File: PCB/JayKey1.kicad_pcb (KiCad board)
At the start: 2 copper layers, 419.1 x 99.4 mm, 204 parts, among them J1 USB_C_Receptacle, K0,0 KEYSW, K0,1 KEYSW, K0,10 KEYSW, K0,11 KEYSW, K0,12 KEYSW, K0,13 KEYSW, K0,14 KEYSW, K0,15 KEYSW, K0,16 KEYSW, K0,17 KEYSW, K0,18 KEYSW, K0,19 KEYSW, K0,2 KEYSW, K0,20 KEYSW, K0,3 KEYSW, K0,4 KEYSW, K0,5 KEYSW, K0,6 KEYSW, K0,7 KEYSW, K0,8 KEYSW, K0,9 KEYSW, K1,0 KEYSW, K1,1 KEYSW, K1,10 KEYSW, K1,11 KEYSW, K1,12 KEYSW, K1,13 KEYSW, K1,14 KEYSW, K1,15 KEYSW, K1,16 KEYSW, K1,17 KEYSW, K1,18 KEYSW, K1,19 KEYSW, K1,2 KEYSW, K1,20 KEYSW, K1,3 KEYSW, K1,4 KEYSW, K1,5 KEYSW, K1,6 KEYSW, K1,7 KEYSW, K1,8 KEYSW, K1,9 KEYSW, K2,0 KEYSW, K2,1 KEYSW, K2,10 KEYSW, K2,11 KEYSW, K2,12 KEYSW, K2,13 KEYSW, K2,14 KEYSW, K2,15 KEYSW, K2,17 KEYSW, K2,18 KEYSW, K2,19 KEYSW, K2,2 KEYSW, K2,20 KEYSW, K2,4 KEYSW, K2,5 KEYSW, K2,6 KEYSW, K2,7 KEYSW, K2,8 KEYSW, K2,9 KEYSW, K3,0 KEYSW, K3,1 KEYSW, K3,10 KEYSW, K3,11 KEYSW, K3,12 KEYSW, K3,13 KEYSW, K3,14 KEYSW, K3,16 KEYSW, K3,18 KEYSW, K3,19 KEYSW, K3,2 KEYSW, K3,20 KEYSW, K3,3 KEYSW, K3,4 KEYSW, K3,5 KEYSW, K3,6 KEYSW, K3,7 KEYSW, K3,8 KEYSW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

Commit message: 2018.04.16 Nightly
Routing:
- net Net-(R_USB3-Pad1): track 194.8 -> 168.7 mm
- net Net-(R_USB4-Pad1): track 192.9 -> 169.5 mm, vias 2 -> 0
- net GND: track 430.8 -> 448.8 mm, vias 12 -> 7
- net /col09: track 137.1 -> 125.2 mm, vias 1 -> 0
- net VCC: track 336.4 -> 327.8 mm
- net /col00: track 317.7 -> 311.5 mm
- net /col12: track 118.0 -> 113.3 mm
- net /col18: track 233.9 -> 230.6 mm, vias 1 -> 2
- net Net-(J1-PadB5): track 61.7 -> 58.9 mm
- net /col03: track 252.4 -> 249.9 mm
- net /col01: track 295.3 -> 292.9 mm
- net Net-(J1-PadA7): track 55.6 -> 53.5 mm
- net Net-(J1-PadA5): track 52.4 -> 50.3 mm
- net Net-(J1-PadA6): track 52.8 -> 50.7 mm
- net /col19: track 252.4 -> 250.7 mm
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
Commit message: 2018.04.20 Update
- Official version 1.0 release
- Cleaned up routing on PCB and moved components for a cleaner design
- Made new constant in matrix.c called 'one' which makes read_cols function easier to read
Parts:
- moved C_REF1 30.4 mm to (287.5, 108.3), turned to 0 degrees
- moved C_VCC1 3.21 mm to (260.2, 110.7)
- moved R_HWB1 3.21 mm to (260.2, 108.3)
- moved C_AVCC1 1.33 mm to (287.5, 110.7)
- moved C_UVCC1 1.33 mm to (287.5, 113.1)
- moved C_VCC2 1.33 mm to (287.5, 106.0)
- moved R_RST1 0.06 mm to (279.2, 120.8), turned to 90 degrees
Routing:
- net GND: track 448.8 -> 408.5 mm, vias 7 -> 4
- net Net-(C_REF1-Pad1): track 28.8 -> 4.93 mm, vias 2 -> 0
- net VCC: track 327.8 -> 322.4 mm, vias 6 -> 2
- net Net-(R_HWB1-Pad2): track 15.7 -> 12.1 mm
- net Net-(R_RST1-Pad1): track 21.4 -> 23.3 mm
- net /row4: track 432.1 -> 433.4 mm, vias 3 -> 2
- net /row3: track 439.4 -> 440.6 mm
- net /col13: track 136.2 -> 135.2 mm
- net /col19: track 250.7 -> 249.9 mm
- net /col14: track 172.3 -> 171.8 mm
- net /col20: track 270.3 -> 269.8 mm
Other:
- board text added: "01001010 01100001 01111001 01001011 01100101 01111001 00110001"
- board text added: "JayKey1 by Josue Galeas (Version 1.0) https://github.com/josuegaleas/JayKey1"

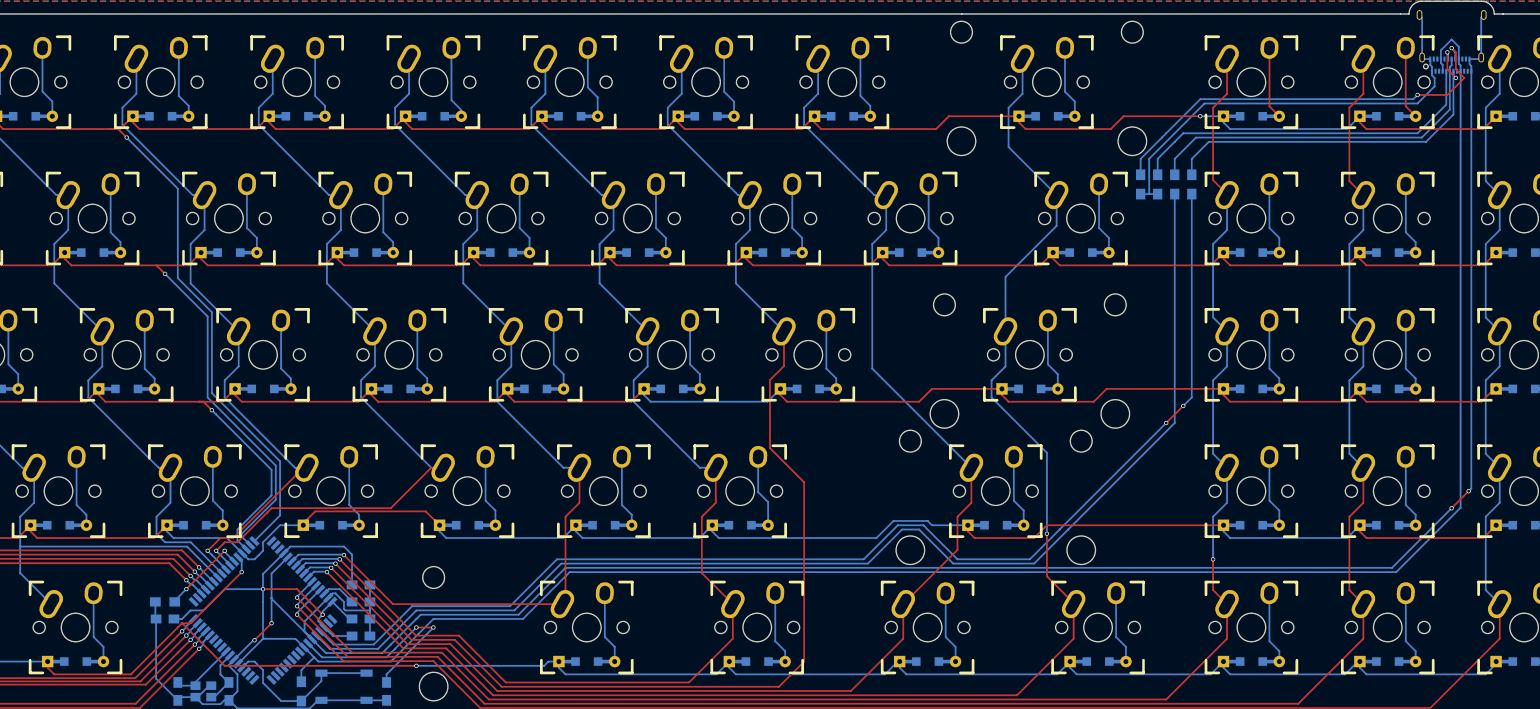
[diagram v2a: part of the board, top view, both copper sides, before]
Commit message: 2018.04.27 Update
- Version 1.1 Release
- Cleaned up routing to the USB port
- Made seperate schematic sheet with key matrix (so it can be used in JayKey2)
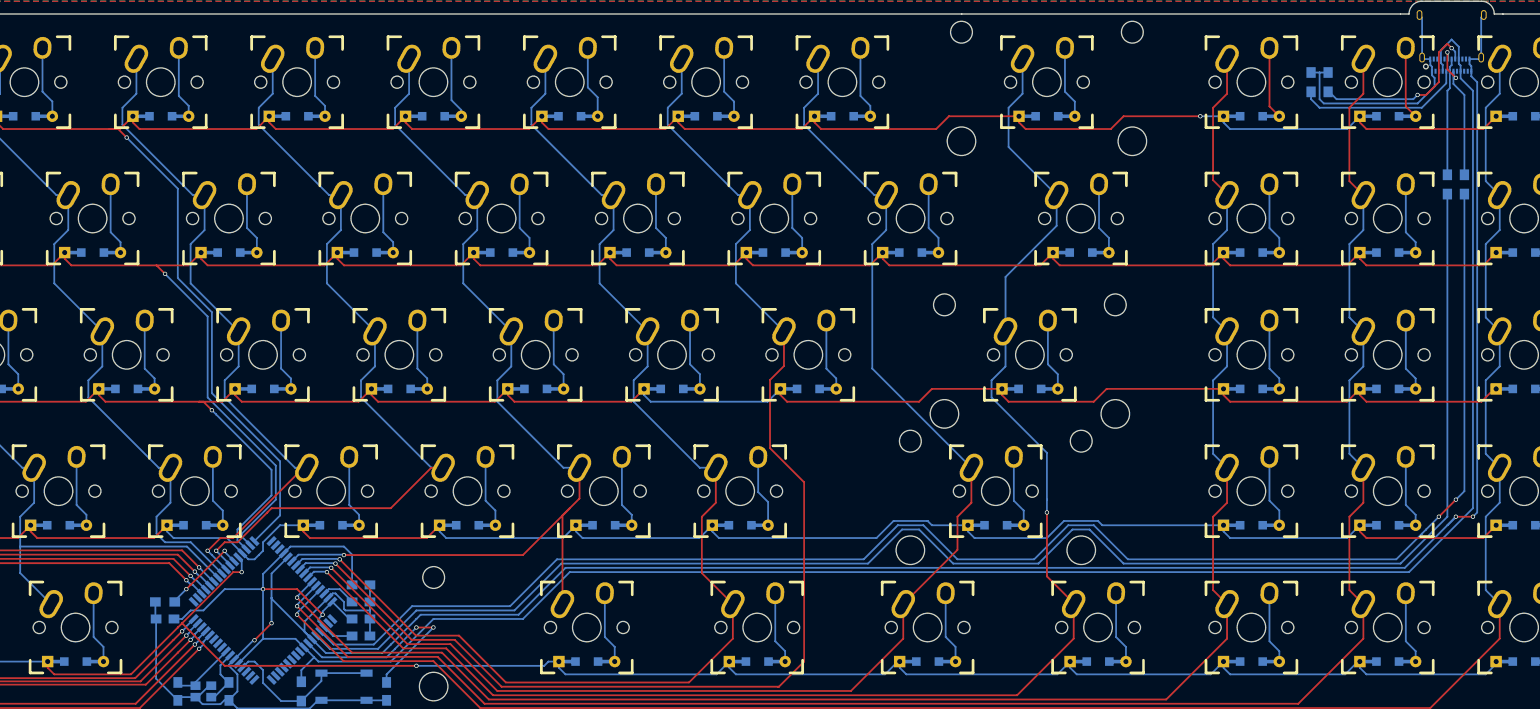
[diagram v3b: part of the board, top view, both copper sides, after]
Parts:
- moved R_USB3 38.1 mm to (441.7, 50.0)
- moved R_USB4 38.1 mm to (439.3, 50.0)
- moved R_USB2 29.8 mm to (422.7, 35.7), turned to 90 degrees
- moved R_USB1 25.8 mm to (420.3, 35.7), turned to 90 degrees
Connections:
- D0,0 pad 1: /row0 -> /Key Matrix/row0
- D0,1 pad 1: /row0 -> /Key Matrix/row0
- D0,10 pad 1: /row0 -> /Key Matrix/row0
- D0,11 pad 1: /row0 -> /Key Matrix/row0
- D0,12 pad 1: /row0 -> /Key Matrix/row0
- D0,13 pad 1: /row0 -> /Key Matrix/row0
- D0,14 pad 1: /row0 -> /Key Matrix/row0
- D0,15 pad 1: /row0 -> /Key Matrix/row0
- D0,16 pad 1: /row0 -> /Key Matrix/row0
- D0,17 pad 1: /row0 -> /Key Matrix/row0
- D0,18 pad 1: /row0 -> /Key Matrix/row0
- D0,19 pad 1: /row0 -> /Key Matrix/row0
- D0,2 pad 1: /row0 -> /Key Matrix/row0
- D0,20 pad 1: /row0 -> /Key Matrix/row0
- D0,3 pad 1: /row0 -> /Key Matrix/row0
- D0,4 pad 1: /row0 -> /Key Matrix/row0
- D0,5 pad 1: /row0 -> /Key Matrix/row0
- D0,6 pad 1: /row0 -> /Key Matrix/row0
- D0,7 pad 1: /row0 -> /Key Matrix/row0
- D0,8 pad 1: /row0 -> /Key Matrix/row0
- D0,9 pad 1: /row0 -> /Key Matrix/row0
- D1,0 pad 1: /row1 -> /Key Matrix/row1
- D1,1 pad 1: /row1 -> /Key Matrix/row1
- D1,10 pad 1: /row1 -> /Key Matrix/row1
- D1,11 pad 1: /row1 -> /Key Matrix/row1
- D1,12 pad 1: /row1 -> /Key Matrix/row1
- D1,13 pad 1: /row1 -> /Key Matrix/row1
- D1,14 pad 1: /row1 -> /Key Matrix/row1
- D1,15 pad 1: /row1 -> /Key Matrix/row1
- D1,16 pad 1: /row1 -> /Key Matrix/row1
- D1,17 pad 1: /row1 -> /Key Matrix/row1
- D1,18 pad 1: /row1 -> /Key Matrix/row1
- D1,19 pad 1: /row1 -> /Key Matrix/row1
- D1,2 pad 1: /row1 -> /Key Matrix/row1
- D1,20 pad 1: /row1 -> /Key Matrix/row1
- D1,3 pad 1: /row1 -> /Key Matrix/row1
- D1,4 pad 1: /row1 -> /Key Matrix/row1
- D1,5 pad 1: /row1 -> /Key Matrix/row1
- D1,6 pad 1: /row1 -> /Key Matrix/row1
- D1,7 pad 1: /row1 -> /Key Matrix/row1
- D1,8 pad 1: /row1 -> /Key Matrix/row1
- D1,9 pad 1: /row1 -> /Key Matrix/row1
- D2,0 pad 1: /row2 -> /Key Matrix/row2
- D2,1 pad 1: /row2 -> /Key Matrix/row2
- D2,10 pad 1: /row2 -> /Key Matrix/row2
- D2,11 pad 1: /row2 -> /Key Matrix/row2
- D2,12 pad 1: /row2 -> /Key Matrix/row2
- D2,13 pad 1: /row2 -> /Key Matrix/row2
- D2,14 pad 1: /row2 -> /Key Matrix/row2
- D2,15 pad 1: /row2 -> /Key Matrix/row2
- D2,17 pad 1: /row2 -> /Key Matrix/row2
- D2,18 pad 1: /row2 -> /Key Matrix/row2
- D2,19 pad 1: /row2 -> /Key Matrix/row2
- D2,2 pad 1: /row2 -> /Key Matrix/row2
- D2,20 pad 1: /row2 -> /Key Matrix/row2
- D2,4 pad 1: /row2 -> /Key Matrix/row2
- D2,5 pad 1: /row2 -> /Key Matrix/row2
- D2,6 pad 1: /row2 -> /Key Matrix/row2
- D2,7 pad 1: /row2 -> /Key Matrix/row2
- D2,8 pad 1: /row2 -> /Key Matrix/row2
- D2,9 pad 1: /row2 -> /Key Matrix/row2
- D3,0 pad 1: /row3 -> /Key Matrix/row3
- D3,1 pad 1: /row3 -> /Key Matrix/row3
- D3,10 pad 1: /row3 -> /Key Matrix/row3
- D3,11 pad 1: /row3 -> /Key Matrix/row3
- D3,12 pad 1: /row3 -> /Key Matrix/row3
- D3,13 pad 1: /row3 -> /Key Matrix/row3
- D3,14 pad 1: /row3 -> /Key Matrix/row3
- D3,16 pad 1: /row3 -> /Key Matrix/row3
- D3,18 pad 1: /row3 -> /Key Matrix/row3
- D3,19 pad 1: /row3 -> /Key Matrix/row3
- D3,2 pad 1: /row3 -> /Key Matrix/row3
- D3,20 pad 1: /row3 -> /Key Matrix/row3
- D3,3 pad 1: /row3 -> /Key Matrix/row3
- D3,4 pad 1: /row3 -> /Key Matrix/row3
- D3,5 pad 1: /row3 -> /Key Matrix/row3
- D3,6 pad 1: /row3 -> /Key Matrix/row3
- D3,7 pad 1: /row3 -> /Key Matrix/row3
- D3,8 pad 1: /row3 -> /Key Matrix/row3
- D3,9 pad 1: /row3 -> /Key Matrix/row3
- D4,0 pad 1: /row4 -> /Key Matrix/row4
- D4,13 pad 1: /row4 -> /Key Matrix/row4
- D4,14 pad 1: /row4 -> /Key Matrix/row4
- D4,16 pad 1: /row4 -> /Key Matrix/row4
- D4,17 pad 1: /row4 -> /Key Matrix/row4
- D4,18 pad 1: /row4 -> /Key Matrix/row4
- D4,19 pad 1: /row4 -> /Key Matrix/row4
- D4,2 pad 1: /row4 -> /Key Matrix/row4
- D4,20 pad 1: /row4 -> /Key Matrix/row4
- D4,4 pad 1: /row4 -> /Key Matrix/row4
- D4,5 pad 1: /row4 -> /Key Matrix/row4
- D4,6 pad 1: /row4 -> /Key Matrix/row4
- D4,9 pad 1: /row4 -> /Key Matrix/row4
- K0,0 pad 1: /col00 -> /Key Matrix/col00
- K0,1 pad 1: /col01 -> /Key Matrix/col01
- K0,10 pad 1: /col10 -> /Key Matrix/col10
- K0,11 pad 1: /col11 -> /Key Matrix/col11
- K0,12 pad 1: /col12 -> /Key Matrix/col12
- K0,13 pad 1: /col13 -> /Key Matrix/col13
- K0,14 pad 1: /col14 -> /Key Matrix/col14
- K0,15 pad 1: /col15 -> /Key Matrix/col15
- K0,16 pad 1: /col16 -> /Key Matrix/col16
- K0,17 pad 1: /col17 -> /Key Matrix/col17
- K0,18 pad 1: /col18 -> /Key Matrix/col18
- K0,19 pad 1: /col19 -> /Key Matrix/col19
- K0,2 pad 1: /col02 -> /Key Matrix/col02
- K0,20 pad 1: /col20 -> /Key Matrix/col20
- K0,3 pad 1: /col03 -> /Key Matrix/col03
- K0,4 pad 1: /col04 -> /Key Matrix/col04
- K0,5 pad 1: /col05 -> /Key Matrix/col05
- K0,6 pad 1: /col06 -> /Key Matrix/col06
- K0,7 pad 1: /col07 -> /Key Matrix/col07
- K0,8 pad 1: /col08 -> /Key Matrix/col08
- K0,9 pad 1: /col09 -> /Key Matrix/col09
- K1,0 pad 1: /col00 -> /Key Matrix/col00
- K1,1 pad 1: /col01 -> /Key Matrix/col01
- K1,10 pad 1: /col10 -> /Key Matrix/col10
- K1,11 pad 1: /col11 -> /Key Matrix/col11
- K1,12 pad 1: /col12 -> /Key Matrix/col12
- K1,13 pad 1: /col13 -> /Key Matrix/col13
- K1,14 pad 1: /col14 -> /Key Matrix/col14
- K1,15 pad 1: /col15 -> /Key Matrix/col15
- K1,16 pad 1: /col16 -> /Key Matrix/col16
- K1,17 pad 1: /col17 -> /Key Matrix/col17
- K1,18 pad 1: /col18 -> /Key Matrix/col18
- K1,19 pad 1: /col19 -> /Key Matrix/col19
- K1,2 pad 1: /col02 -> /Key Matrix/col02
- K1,20 pad 1: /col20 -> /Key Matrix/col20
- K1,3 pad 1: /col03 -> /Key Matrix/col03
- K1,4 pad 1: /col04 -> /Key Matrix/col04
- K1,5 pad 1: /col05 -> /Key Matrix/col05
- K1,6 pad 1: /col06 -> /Key Matrix/col06
- K1,7 pad 1: /col07 -> /Key Matrix/col07
- K1,8 pad 1: /col08 -> /Key Matrix/col08
- K1,9 pad 1: /col09 -> /Key Matrix/col09
- K2,0 pad 1: /col00 -> /Key Matrix/col00
- K2,1 pad 1: /col01 -> /Key Matrix/col01
- K2,10 pad 1: /col10 -> /Key Matrix/col10
- K2,11 pad 1: /col11 -> /Key Matrix/col11
- K2,12 pad 1: /col12 -> /Key Matrix/col12
- K2,13 pad 1: /col13 -> /Key Matrix/col13
- K2,14 pad 1: /col14 -> /Key Matrix/col14
- K2,15 pad 1: /col15 -> /Key Matrix/col15
- K2,17 pad 1: /col17 -> /Key Matrix/col17
- K2,18 pad 1: /col18 -> /Key Matrix/col18
- K2,19 pad 1: /col19 -> /Key Matrix/col19
- K2,2 pad 1: /col02 -> /Key Matrix/col02
- K2,20 pad 1: /col20 -> /Key Matrix/col20
- K2,4 pad 1: /col04 -> /Key Matrix/col04
- K2,5 pad 1: /col05 -> /Key Matrix/col05
- K2,6 pad 1: /col06 -> /Key Matrix/col06
- K2,7 pad 1: /col07 -> /Key Matrix/col07
- K2,8 pad 1: /col08 -> /Key Matrix/col08
- K2,9 pad 1: /col09 -> /Key Matrix/col09
- K3,0 pad 1: /col00 -> /Key Matrix/col00
- K3,1 pad 1: /col01 -> /Key Matrix/col01
- K3,10 pad 1: /col10 -> /Key Matrix/col10
- K3,11 pad 1: /col11 -> /Key Matrix/col11
- K3,12 pad 1: /col12 -> /Key Matrix/col12
- K3,13 pad 1: /col13 -> /Key Matrix/col13
- K3,14 pad 1: /col14 -> /Key Matrix/col14
- K3,16 pad 1: /col16 -> /Key Matrix/col16
- K3,18 pad 1: /col18 -> /Key Matrix/col18
- K3,19 pad 1: /col19 -> /Key Matrix/col19
- K3,2 pad 1: /col02 -> /Key Matrix/col02
- K3,20 pad 1: /col20 -> /Key Matrix/col20
- K3,3 pad 1: /col03 -> /Key Matrix/col03
- K3,4 pad 1: /col04 -> /Key Matrix/col04
- K3,5 pad 1: /col05 -> /Key Matrix/col05
- K3,6 pad 1: /col06 -> /Key Matrix/col06
- K3,7 pad 1: /col07 -> /Key Matrix/col07
- K3,8 pad 1: /col08 -> /Key Matrix/col08
- K3,9 pad 1: /col09 -> /Key Matrix/col09
- K4,0 pad 1: /col00 -> /Key Matrix/col00
- K4,13 pad 1: /col13 -> /Key Matrix/col13
- K4,14 pad 1: /col14 -> /Key Matrix/col14
- K4,16 pad 1: /col16 -> /Key Matrix/col16
- K4,17 pad 1: /col17 -> /Key Matrix/col17
- K4,18 pad 1: /col18 -> /Key Matrix/col18
- K4,19 pad 1: /col19 -> /Key Matrix/col19
- K4,2 pad 1: /col02 -> /Key Matrix/col02
- K4,20 pad 1: /col20 -> /Key Matrix/col20
- K4,4 pad 1: /col04 -> /Key Matrix/col04
- K4,5 pad 1: /col05 -> /Key Matrix/col05
- K4,6 pad 1: /col06 -> /Key Matrix/col06
- K4,9 pad 1: /col09 -> /Key Matrix/col09
- U1 pad 28: /col00 -> (no net)
- U1 pad 29: /col01 -> (no net)
- U1 pad 30: /col02 -> (no net)
- U1 pad 31: /col03 -> (no net)
- U1 pad 32: /col04 -> (no net)
- U1 pad 35: /col05 -> (no net)
- U1 pad 36: /col06 -> (no net)
- U1 pad 37: /col07 -> (no net)
- U1 pad 38: /col08 -> (no net)
- U1 pad 39: /col09 -> (no net)
- U1 pad 40: /col10 -> (no net)
- U1 pad 41: /col11 -> (no net)
- U1 pad 42: /col12 -> (no net)
- U1 pad 44: /row4 -> (no net)
- U1 pad 45: /row3 -> (no net)
- U1 pad 46: /row2 -> (no net)
- U1 pad 47: /row1 -> (no net)
- U1 pad 48: /row0 -> (no net)
- U1 pad 54: /col13 -> (no net)
- U1 pad 55: /col14 -> (no net)
- U1 pad 56: /col15 -> (no net)
- U1 pad 57: /col16 -> (no net)
- U1 pad 58: /col17 -> (no net)
- U1 pad 59: /col18 -> (no net)
- U1 pad 60: /col19 -> (no net)
- U1 pad 61: /col20 -> (no net)
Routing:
- net /row0: track 508.4 -> 0.00 mm, vias 2 -> 0
- net /Key Matrix/row0: track 0.00 -> 508.4 mm, vias 0 -> 2
- net /row1: track 487.7 -> 0.00 mm, vias 1 -> 0
- net /Key Matrix/row1: track 0.00 -> 487.7 mm, vias 0 -> 1
- net /row2: track 463.4 -> 0.00 mm, vias 1 -> 0
- net /Key Matrix/row2: track 0.00 -> 463.4 mm, vias 0 -> 1
- net /row3: track 440.6 -> 0.00 mm, vias 1 -> 0
- net /Key Matrix/row3: track 0.00 -> 440.5 mm, vias 0 -> 1
- net /row4: track 433.4 -> 0.00 mm, vias 2 -> 0
- net /Key Matrix/row4: track 0.00 -> 432.6 mm, vias 0 -> 2
- net /col00: track 311.1 -> 0.00 mm, vias 1 -> 0
- net /Key Matrix/col00: track 0.00 -> 311.1 mm, vias 0 -> 1
- net /col01: track 292.6 -> 0.00 mm, vias 1 -> 0
- net /Key Matrix/col01: track 0.00 -> 292.6 mm, vias 0 -> 1
- net /col02: track 282.0 -> 0.00 mm, vias 1 -> 0
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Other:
- board text added: "JayKey1 by Josue Galeas (Version 1.1) https://github.com/josuegaleas/JayKey1"
- board text removed: "JayKey1 by Josue Galeas (Version 1.0) https://github.com/josuegaleas/JayKey1"

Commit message: 2018.08.27 Nightly
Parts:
- added C_VBUS1: 10u, Capacitors_SMD:C_0805_HandSoldering, B.Cu at (294.1, 120.8)
- added J2: USB_C_Receptacle, Connectors_USB:USB_C_Receptacle_Amphenol_12401610E4-2A, B.Cu at (58.9, 29.2)
- added R_USB5: 5.1k, Resistors_SMD:R_0805_HandSoldering, B.Cu at (54.8, 46.4)
- added R_USB6: 5.1k, Resistors_SMD:R_0805_HandSoldering, B.Cu at (54.8, 44.1)
- added R_USB7: 22, Resistors_SMD:R_0805_HandSoldering, B.Cu at (60.7, 50.0)
- added R_USB8: 22, Resistors_SMD:R_0805_HandSoldering, B.Cu at (58.3, 50.0)
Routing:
- net GND: track 385.3 -> 439.1 mm
- net Net-(J2-PadA7): track 0.00 -> 21.2 mm, vias 0 -> 2
- net Net-(J2-PadB5): track 0.00 -> 17.5 mm, vias 0 -> 2
- net Net-(J2-PadA6): track 0.00 -> 16.4 mm
- net VCC: track 324.9 -> 339.8 mm
- net Net-(J2-PadA5): track 0.00 -> 13.1 mm
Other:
- outline, holes or cut-outs redrawn
- board text removed: "01001010 01100001 01111001 01001011 01100101 01111001 00110001"

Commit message: 2018.09.29 Nightly
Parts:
- removed C_CAP1: 1u, Capacitors_SMD:C_0805_HandSoldering
- removed C_REF1: 100n, Capacitors_SMD:C_0805_HandSoldering
- removed R_USB7, R_USB8: 22, Resistors_SMD:R_0805_HandSoldering
- added C_AREF1: 100n, Capacitors_SMD:C_0805_HandSoldering, B.Cu at (287.5, 108.3)
- added C_UCAP1: 1u, Capacitors_SMD:C_0805_HandSoldering, B.Cu at (291.1, 120.8)
- added D_ESD1: PESD5V0L2BT, TO_SOT_Packages_SMD:SOT-23, B.Cu at (444.1, 17.9)
- added D_ESD2: PESD5V0L2BT, TO_SOT_Packages_SMD:SOT-23, B.Cu at (58.9, 39.3)
- added D_VBUS1: D, keyboard_parts:D_SOD123_axial, B.Cu at (457.8, 16.7)
- added D_VBUS2: D, keyboard_parts:D_SOD123_axial, B.Cu at (61.3, 52.4)
- C_UVCC1: value 1u -> 100n
- R_RST1: value 10k -> 47k
- R_USB1, R_USB2: value 5.1k -> 22
- R_USB3, R_USB4: value 22 -> 5.1k
- U1: value AT90USB1286 -> AT90USB1286-AU
- moved R_USB2 176.0 mm to (277.4, 135.1)
- moved R_USB1 176.0 mm to (275.0, 135.1)
- moved R_USB3 32.8 mm to (431.0, 19.1)
- moved R_USB4 32.8 mm to (428.6, 19.1)
- moved J1 0.60 mm to (439.9, 28.6)
- moved J2 0.60 mm to (58.9, 28.6)
- moved R_USB5 0.60 mm to (54.2, 46.4)
- moved R_USB6 0.60 mm to (54.2, 44.1)
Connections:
- J1 pad A4: VCC -> Net-(D_VBUS1-Pad2)
- J1 pad A6: Net-(J1-PadA6) -> /DPLUS
- J1 pad A7: Net-(J1-PadA7) -> /DMINUS
- J1 pad A9: VCC -> Net-(D_VBUS1-Pad2)
- J1 pad B4: VCC -> Net-(D_VBUS1-Pad2)
- J1 pad B6: Net-(J1-PadA6) -> /DPLUS
- J1 pad B7: Net-(J1-PadA7) -> /DMINUS
- J1 pad B9: VCC -> Net-(D_VBUS1-Pad2)
- J2 pad A4: VCC -> Net-(D_VBUS2-Pad2)
- J2 pad A6: Net-(J2-PadA6) -> /DPLUS
- J2 pad A7: Net-(J2-PadA7) -> /DMINUS
- J2 pad A9: VCC -> Net-(D_VBUS2-Pad2)
- J2 pad B4: VCC -> Net-(D_VBUS2-Pad2)
- J2 pad B6: Net-(J2-PadA6) -> /DPLUS
- J2 pad B7: Net-(J2-PadA7) -> /DMINUS
- J2 pad B9: VCC -> Net-(D_VBUS2-Pad2)
- R_USB1 pad 1: Net-(J1-PadA5) -> Net-(R_USB1-Pad1)
- R_USB1 pad 2: GND -> /DMINUS
- R_USB2 pad 1: Net-(J1-PadB5) -> Net-(R_USB2-Pad1)
- R_USB2 pad 2: GND -> /DPLUS
- R_USB3 pad 1: Net-(R_USB3-Pad1) -> Net-(J1-PadA5)
- R_USB3 pad 2: Net-(J1-PadA7) -> GND
- R_USB4 pad 1: Net-(R_USB4-Pad1) -> Net-(J1-PadB5)
- R_USB4 pad 2: Net-(J1-PadA6) -> GND
- U1 pad 23: Net-(C_CLK2-Pad1) -> Net-(C_CLK1-Pad1)
- U1 pad 24: Net-(C_CLK1-Pad1) -> Net-(C_CLK2-Pad1)
- U1 pad 4: Net-(R_USB3-Pad1) -> Net-(R_USB1-Pad1)
- U1 pad 5: Net-(R_USB4-Pad1) -> Net-(R_USB2-Pad1)
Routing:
- net Net-(R_USB2-Pad1): track 0.00 -> 219.5 mm
- net Net-(R_USB4-Pad1): track 219.5 -> 0.00 mm
- net Net-(R_USB3-Pad1): track 218.9 -> 0.00 mm, vias 2 -> 0
- net Net-(R_USB1-Pad1): track 0.00 -> 218.9 mm, vias 0 -> 2
- net GND: track 439.1 -> 397.2 mm, vias 4 -> 6
- net /DMINUS: track 0.00 -> 38.6 mm, vias 0 -> 2
- net /DPLUS: track 0.00 -> 32.2 mm
- net Net-(D_VBUS2-Pad2): track 0.00 -> 27.3 mm
- net Net-(J1-PadB5): track 25.3 -> 0.00 mm, vias 2 -> 0
- net Net-(J1-PadA5): track 23.5 -> 0.00 mm
- net Net-(J2-PadA7): track 21.2 -> 0.00 mm, vias 2 -> 0
- net Net-(J1-PadA7): track 21.2 -> 0.00 mm, vias 2 -> 0
- net Net-(J1-PadA6): track 16.4 -> 0.00 mm
- net Net-(J2-PadA6): track 16.4 -> 0.00 mm
- net VCC: track 339.8 -> 325.3 mm
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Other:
- board size 419.1 x 99.4 mm -> 419.1 x 101.2 mm
- board text added: "JayKey1 by Josue Galeas (Version 1.2) https://github.com/josuegaleas/JayKey1"
- board text removed: "JayKey1 by Josue Galeas (Version 1.1) https://github.com/josuegaleas/JayKey1"

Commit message: 2018.10.02 Nightly
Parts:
- J1, J2: footprint Connectors_USB:USB_C_Receptacle_Amphenol_12401610E4-2A -> Connector_USB:USB_C_Receptacle_Amphenol_12401610E4-2A

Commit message: 2018.10.11 Nightly
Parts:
- moved D_VBUS1 38.9 mm to (442.3, 52.4), turned to 90 degrees
- moved R_USB3 27.7 mm to (435.3, 46.4), turned to 180 degrees
- moved R_USB4 25.9 mm to (435.3, 44.1), turned to 180 degrees
- moved D_ESD1 21.8 mm to (439.9, 39.3), turned to 90 degrees
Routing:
- net Net-(D_VBUS1-Pad2): track 0.00 -> 29.6 mm
- net GND: track 397.2 -> 420.2 mm, vias 6 -> 8
- net VCC: track 325.3 -> 303.5 mm
- net Net-(J1-PadB5): track 0.00 -> 19.2 mm, vias 0 -> 2
- net Net-(J1-PadA5): track 0.00 -> 13.9 mm
- net /DMINUS: track 38.6 -> 52.5 mm, vias 2 -> 4
- net Net-(R_USB2-Pad1): track 219.5 -> 207.7 mm
- net Net-(R_USB1-Pad1): track 218.9 -> 207.2 mm
- net /DPLUS: track 32.2 -> 41.0 mm
- net Net-(C_CLK1-Pad1): track 12.4 -> 5.06 mm
- net /Key Matrix/col10: track 95.3 -> 89.1 mm
- net /Key Matrix/col09: track 124.9 -> 118.8 mm
- net /Key Matrix/row0: track 508.4 -> 503.3 mm
- net /Key Matrix/col20: track 269.8 -> 265.2 mm
- net /Key Matrix/row3: track 440.5 -> 436.3 mm
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
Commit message: 2018.10.25 Nightly
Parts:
- D_ESD1, D_ESD2: footprint TO_SOT_Packages_SMD:SOT-23 -> Package_TO_SOT_SMD:SOT-23_Handsoldering
- J1, J2: value USB_C_Receptacle -> USB_C_Receptacle_USB2.0
- SW1: footprint Buttons_Switches_SMD:SW_SPST_TL3342 -> Button_Switch_SMD:SW_SPST_TL3342
- U1: footprint Housings_QFP:TQFP-64_14x14mm_Pitch0.8mm -> Package_QFP:TQFP-64_14x14mm_P0.8mm
- Y1: footprint Crystals:Crystal_SMD_SeikoEpson_FA238-4pin_3.2x2.5mm -> Crystal:Crystal_SMD_SeikoEpson_FA238-4Pin_3.2x2.5mm_HandSoldering
- moved C_CLK1 9.27 mm to (257.8, 129.1)
- moved Y1 9.07 mm to (261.9, 129.2)
- moved C_CLK2 8.79 mm to (266.1, 129.1)
- moved D_ESD1 1.19 mm to (439.9, 40.5)
- moved D_ESD2 1.19 mm to (58.9, 40.5)
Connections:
- C_AVCC1 pad 1: VCC -> VBUS
- C_UVCC1 pad 1: VCC -> VBUS
- C_VBUS1 pad 1: VCC -> VBUS
- C_VCC1 pad 1: VCC -> VBUS
- C_VCC2 pad 1: VCC -> VBUS
- D_VBUS1 pad 1: VCC -> VBUS
- D_VBUS1 pad 2: Net-(D_VBUS1-Pad2) -> VBUS
- D_VBUS2 pad 1: VCC -> VBUS
- D_VBUS2 pad 2: Net-(D_VBUS2-Pad2) -> VBUS
- J1 pad A4: Net-(D_VBUS1-Pad2) -> VBUS
- J1 pad A8: (no net) -> Net-(J1-PadA8)
- J1 pad A9: Net-(D_VBUS1-Pad2) -> VBUS
- J1 pad B4: Net-(D_VBUS1-Pad2) -> VBUS
- J1 pad B8: (no net) -> Net-(J1-PadB8)
- J1 pad B9: Net-(D_VBUS1-Pad2) -> VBUS
- J2 pad A4: Net-(D_VBUS2-Pad2) -> VBUS
- J2 pad A8: (no net) -> Net-(J2-PadA8)
- J2 pad A9: Net-(D_VBUS2-Pad2) -> VBUS
- J2 pad B4: Net-(D_VBUS2-Pad2) -> VBUS
- J2 pad B8: (no net) -> Net-(J2-PadB8)
- J2 pad B9: Net-(D_VBUS2-Pad2) -> VBUS
- R_RST1 pad 2: VCC -> VBUS
- U1 pad 1: (no net) -> Net-(U1-Pad1)
- U1 pad 10: (no net) -> Net-(U1-Pad10)
- U1 pad 11: (no net) -> Net-(U1-Pad11)
- U1 pad 12: (no net) -> Net-(U1-Pad12)
- U1 pad 13: (no net) -> Net-(U1-Pad13)
- U1 pad 14: (no net) -> Net-(U1-Pad14)
- U1 pad 15: (no net) -> Net-(U1-Pad15)
- U1 pad 16: (no net) -> Net-(U1-Pad16)
- U1 pad 17: (no net) -> Net-(U1-Pad17)
- U1 pad 18: (no net) -> Net-(U1-Pad18)
- U1 pad 19: (no net) -> Net-(U1-Pad19)
- U1 pad 2: (no net) -> Net-(U1-Pad2)
- U1 pad 21: VCC -> VBUS
- U1 pad 25: (no net) -> Net-(U1-Pad25)
- U1 pad 26: (no net) -> Net-(U1-Pad26)
- U1 pad 27: (no net) -> Net-(U1-Pad27)
- U1 pad 28: (no net) -> /col00
- U1 pad 29: (no net) -> /col01
- U1 pad 3: VCC -> VBUS
- U1 pad 30: (no net) -> /col02
- U1 pad 31: (no net) -> /col03
- U1 pad 32: (no net) -> /col04
- U1 pad 33: (no net) -> Net-(U1-Pad33)
- U1 pad 34: (no net) -> Net-(U1-Pad34)
- U1 pad 35: (no net) -> /col05
- U1 pad 36: (no net) -> /col06
- U1 pad 37: (no net) -> /col07
- U1 pad 38: (no net) -> /col08
- U1 pad 39: (no net) -> /col09
- U1 pad 40: (no net) -> /col10
- U1 pad 41: (no net) -> /col11
- U1 pad 42: (no net) -> /col12
- U1 pad 44: (no net) -> /row4
- U1 pad 45: (no net) -> /row3
- U1 pad 46: (no net) -> /row2
- U1 pad 47: (no net) -> /row1
- U1 pad 48: (no net) -> /row0
- U1 pad 49: (no net) -> Net-(U1-Pad49)
- U1 pad 50: (no net) -> Net-(U1-Pad50)
- U1 pad 51: (no net) -> Net-(U1-Pad51)
- U1 pad 52: VCC -> VBUS
- U1 pad 54: (no net) -> /col13
- U1 pad 55: (no net) -> /col14
- U1 pad 56: (no net) -> /col15
- U1 pad 57: (no net) -> /col16
- U1 pad 58: (no net) -> /col17
- U1 pad 59: (no net) -> /col18
- U1 pad 60: (no net) -> /col19
- U1 pad 61: (no net) -> /col20
- U1 pad 64: VCC -> VBUS
- U1 pad 8: VCC -> VBUS
- U1 pad 9: (no net) -> Net-(U1-Pad9)
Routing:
- net VBUS: track 0.00 -> 360.5 mm, vias 0 -> 2
- net VCC: track 303.5 -> 0.00 mm, vias 2 -> 0
- net Net-(D_VBUS1-Pad2): track 29.6 -> 0.00 mm
- net GND: track 420.2 -> 391.5 mm
- net Net-(D_VBUS2-Pad2): track 27.3 -> 0.00 mm
- net Net-(C_CLK1-Pad1): track 5.06 -> 0.00 mm
- net Net-(C_CLK2-Pad1): track 3.38 -> 0.00 mm
- net /DMINUS: track 52.5 -> 54.2 mm
- net /DPLUS: track 41.0 -> 42.7 mm
- net Net-(R_RST1-Pad1): track 23.3 -> 23.8 mm
